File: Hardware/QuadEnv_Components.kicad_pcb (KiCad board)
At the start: 2 copper layers, 18.8 x 110 mm, 50 parts, among them J1 Eurorack_10_pin_power, J2 Conn_01x04_Male, J3 Conn_01x04_Male, J4 Conn_01x04_Male, J5 Conn_01x04_Male, U1 STM32C031C6T, U2 LD1117-3.3-4Tab, U3 TL074

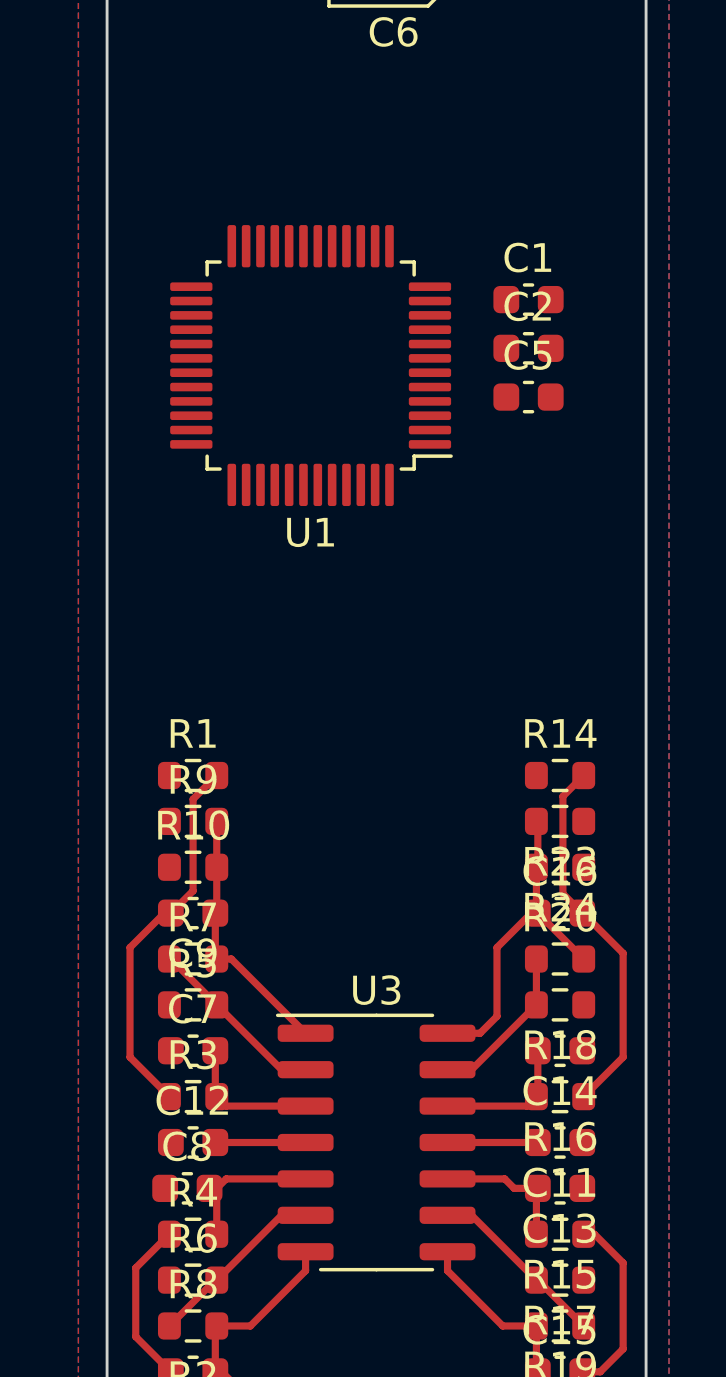
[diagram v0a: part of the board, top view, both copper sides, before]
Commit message: Started adding UART
Though tests show that UART1 is not connected by default on Nucleo
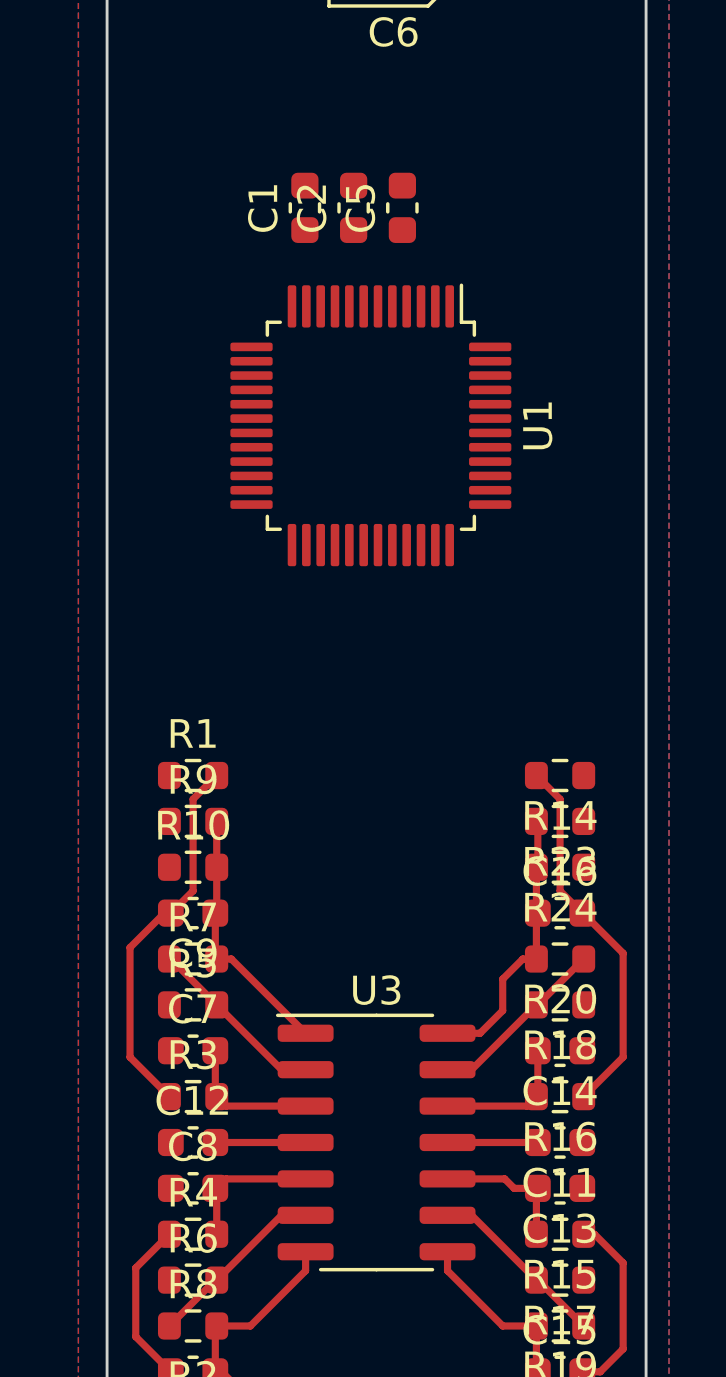
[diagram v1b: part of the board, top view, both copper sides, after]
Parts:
- moved C1 8.43 mm to (56.9, 93.4), turned to 90 degrees
- moved C5 7.93 mm to (60.3, 93.4), turned to 90 degrees
- moved C2 7.82 mm to (58.6, 93.4), turned to 90 degrees
- moved U1 2.97 mm to (59.2, 101.0), turned to -90 degrees
- moved C8 0.20 mm to (53.0, 127.6)
- turned R14 to 180 degrees
- turned R20 to 180 degrees
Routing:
- net Net-(C16-Pad1): track 11.8 -> 9.88 mm
- net Net-(R18-Pad2): track 5.64 -> 6.35 mm
